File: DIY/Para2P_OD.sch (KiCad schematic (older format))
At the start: 8 parts, among them J1 Atari_SEGA_DE9, J2 Atari_SEGA_DE9, J3 DB25_Male, U1 74AHCT125N, U2 74AHCT125N, U3 74AHCT125N

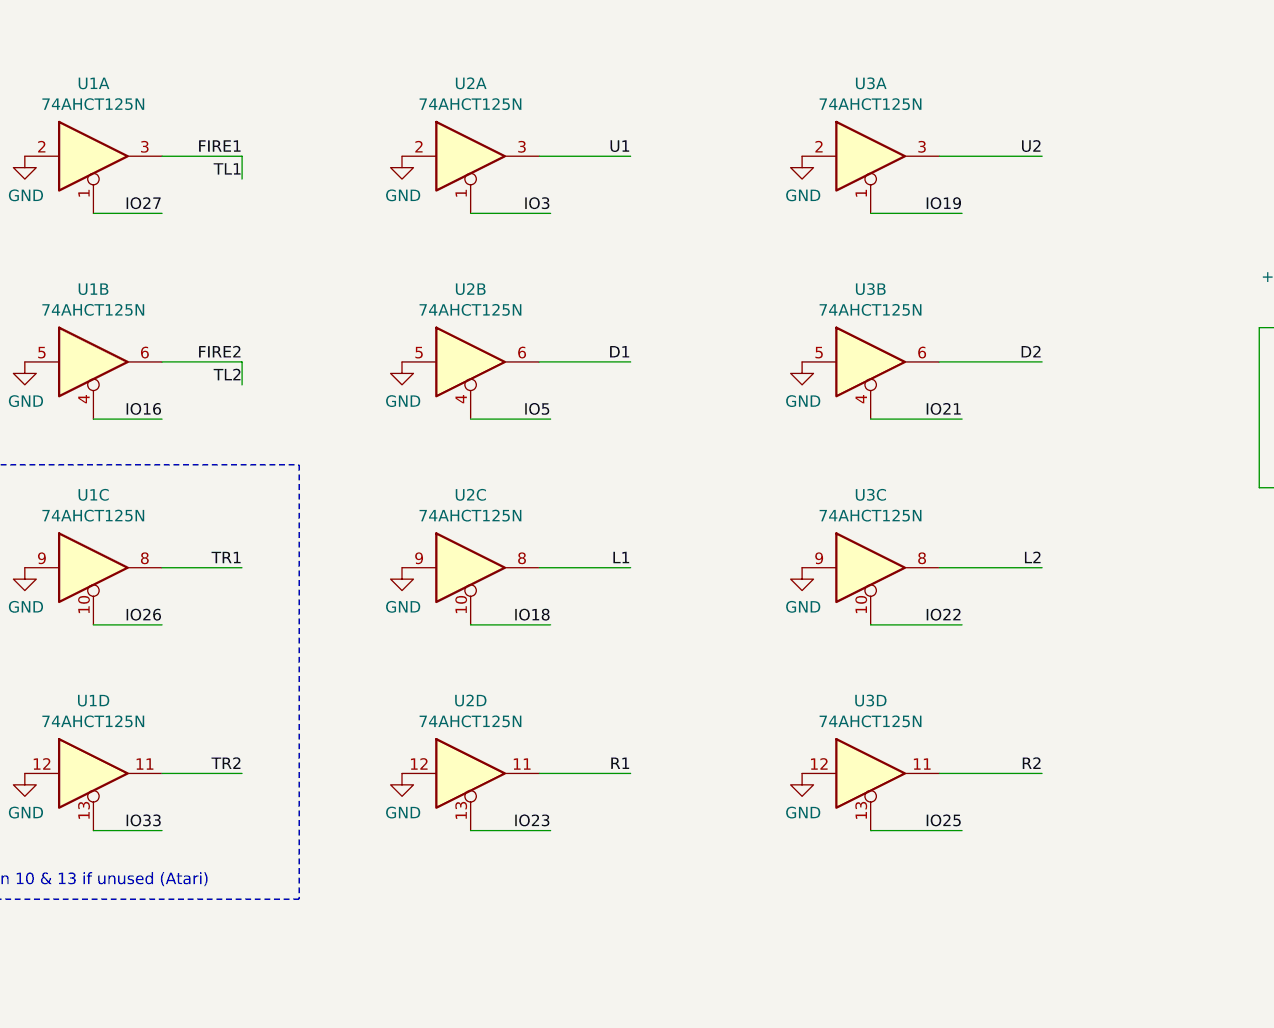
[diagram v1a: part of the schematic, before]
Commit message: Add pullup to OD outputs on ESP side
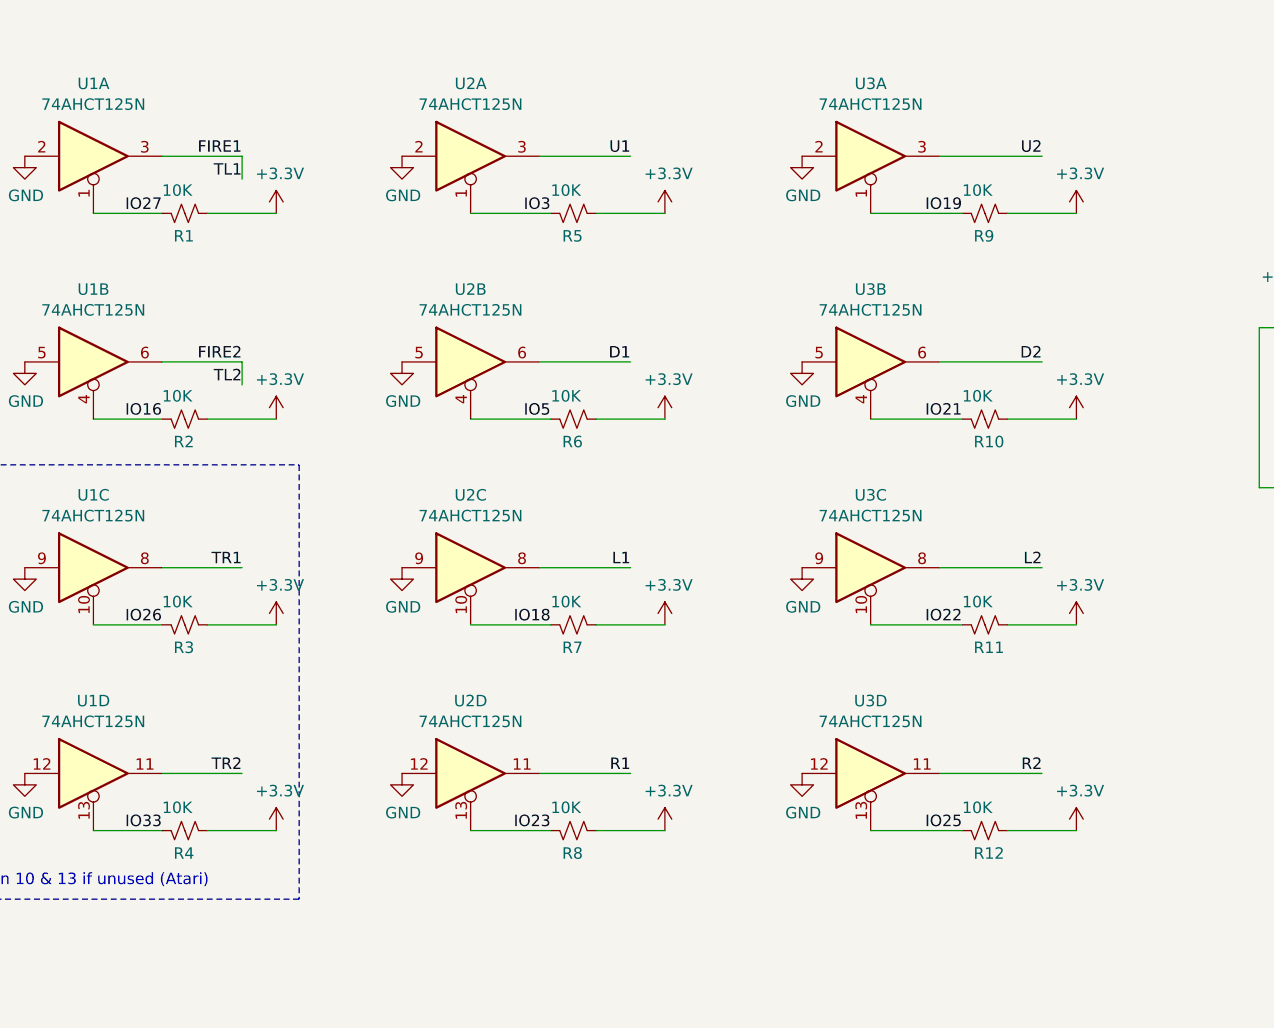
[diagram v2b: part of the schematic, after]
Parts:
- added R1, R10, R11, R12, R2, R3, R4, R5, R6, R7, R8, R9: 10K, symbol Device:R_Small_US
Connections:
- net +3V3: now also R1.1, R10.1, R11.1, R12.1, R2.1, R3.1, R4.1, R5.1, R6.1, R7.1, R8.1, R9.1
- net IO16: now also R2.2
- net IO18: now also R7.2
- net IO19: now also R9.2
- net IO21: now also R10.2
- net IO22: now also R11.2
- net IO23: now also R8.2
- net IO25: now also R12.2
- net IO26: now also R3.2
- net IO27: now also R1.2
- net IO3: now also R5.2
- net IO33: now also R4.2
- net IO5: now also R6.2
